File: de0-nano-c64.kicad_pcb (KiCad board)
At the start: 2 copper layers, 79.4 x 75.3 mm, 51 parts, among them J1 GPIO_0, J10 SD_Card, J11 AUDIO, J2 PS2_0, J3 PS2_1, J5 GPIO_1, J6 VGA, J8 JOYSTICK_1, J9 JOYSTICK_2

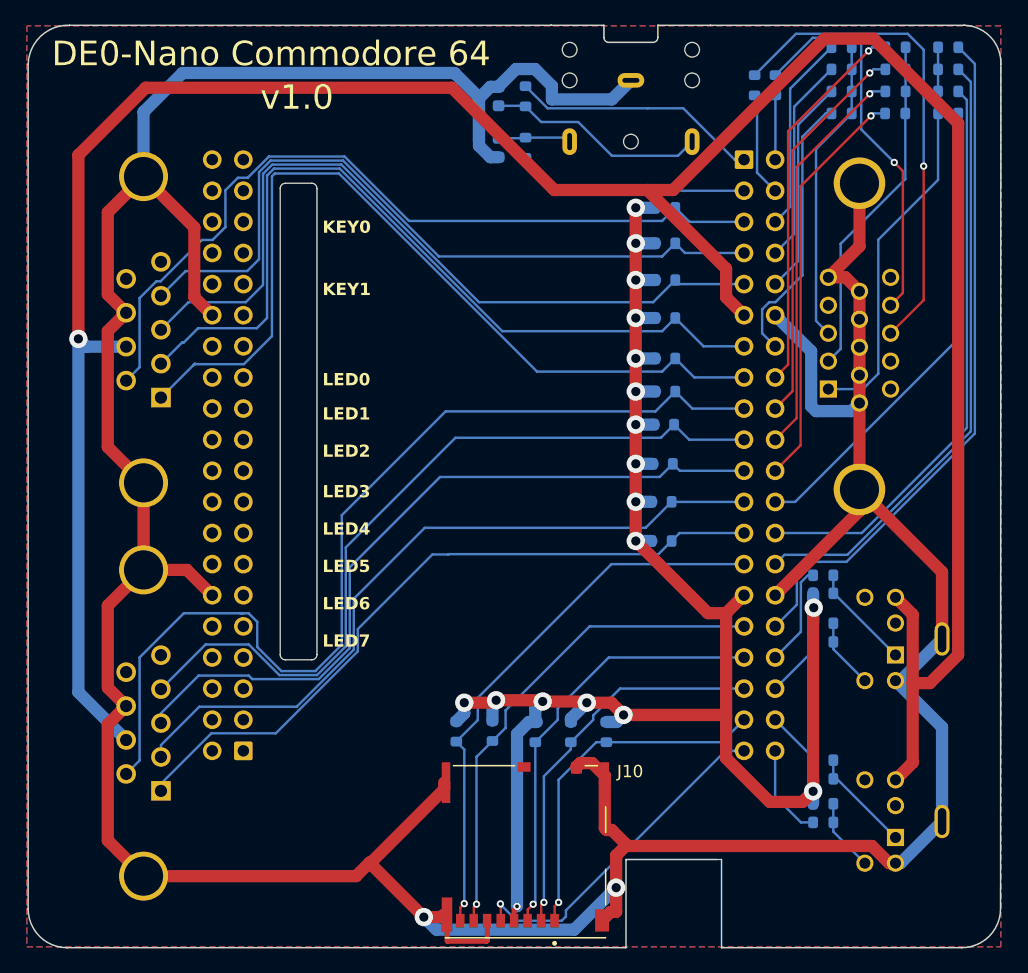
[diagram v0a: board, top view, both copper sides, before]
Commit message: reorder some pins due to input only problem
audio PWM_L/R were assigne to input only pins
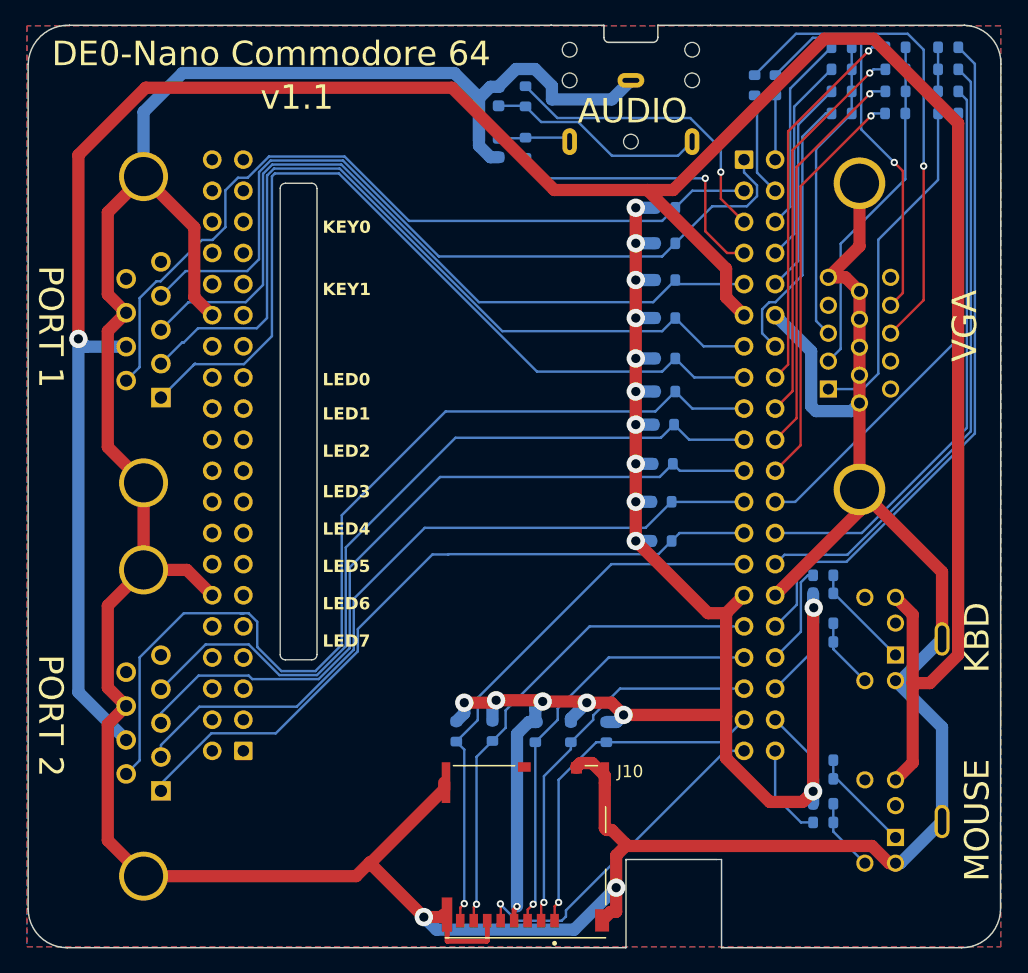
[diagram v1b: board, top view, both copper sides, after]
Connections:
- J5 pad 1: /PWM_L -> /J1_RIGHT
- J5 pad 3: /PWM_R -> /J1_FIRE
- J5 pad 5: /J1_FIRE -> /PWM_L
- J5 pad 7: /J1_RIGHT -> /PWM_R
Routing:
- net /J1_RIGHT: track 60.3 -> 66.1 mm
- net /PWM_R: track 18.9 -> 23.6 mm, vias 0 -> 1
- net /PWM_L: track 20.3 -> 24.8 mm, vias 0 -> 1
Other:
- board text added: "AUDIO"
- board text added: "KBD"
- board text added: "MOUSE"
- board text added: "PORT 1"
- board text added: "PORT 2"
- board text added: "VGA"
- board text added: "v1.1"
- board text removed: "v1.0"
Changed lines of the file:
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@@
       (stroke (width 0.1) (type solid)) (layer "B.Fab"))
     (pad "1" thru_hole roundrect (at 0 0 180) (size 1.524 1.524) (drill 0.9398) (layers "*.Cu" "*.Mask") (roundrect_rratio 0.1)
-      (net 80 "/PWM_L") (pinfunction "Pin_1") (pintype "passive"))
+      (net 67 "/J1_RIGHT") (pinfunction "Pin_1") (pintype "passive"))
     (pad "2" thru_hole circle (at -2.54 0 180) (size 1.524 1.524) (drill 0.9398) (layers "*.Cu" "*.Mask")
       (net 13 "/VS") (pinfunction "Pin_2") (pintype "passive"))
     (pad "3" thru_hole circle (at 0 -2.54 180) (size 1.524 1.524) (drill 0.9398) (layers "*.Cu" "*.Mask")
-      (net 81 "/PWM_R") (pinfunction "Pin_3") (pintype "passive"))
+      (net 68 "/J1_FIRE") (pinfunction "Pin_3") (pintype "passive"))
     (pad "4" thru_hole circle (at -2.54 -2.54 180) (size 1.524 1.524) (drill 0.9398) (layers "*.Cu" "*.Mask")
       (net 12 "/HS") (pinfunction "Pin_4") (pintype "passive"))
     (pad "5" thru_hole circle (at 0 -5.08 180) (size 1.524 1.524) (drill 0.9398) (layers "*.Cu" "*.Mask")
-      (net 68 "/J1_FIRE") (pinfunction "Pin_5") (pintype "passive"))
+      (net 80 "/PWM_L") (pinfunction "Pin_5") (pintype "passive"))
     (pad "6" thru_hole circle (at -2.54 -5.08 180) (size 1.524 1.524) (drill 0.9398) (layers "*.Cu" "*.Mask")
       (net 11 "/B0") (pinfunction "Pin_6") (pintype "passive"))
     (pad "7" thru_hole circle (at 0 -7.62 180) (size 1.524 1.524) (drill 0.9398) (layers "*.Cu" "*.Mask")
-      (net 67 "/J1_RIGHT") (pinfunction "Pin_7") (pintype "passive"))
+      (net 81 "/PWM_R") (pinfunction "Pin_7") (pintype "passive"))
     (pad "8" thru_hole circle (at -2.54 -7.62 180) (size 1.524 1.524) (drill 0.9398) (layers "*.Cu" "*.Mask")
       (net 9 "/B1") (pinfunction "Pin_8") (pintype "passive"))
@@
   (gr_line (start 125.767499 117.240001) (end 125.76802 79.19052)
     (stroke (width 0.05) (type default)) (layer "Edge.Cuts"))
+  (gr_text "PORT 2" (at 105.8545 117.221 270) (layer "F.SilkS")
+    (effects (font (size 2 2) (thickness 0.3)) (justify left bottom))
+  )
   (gr_text "LED6" (at 129.2225 113.665) (layer "F.SilkS")
     (effects (font (size 1 1) (thickness 0.15) bold) (justify left bottom))
   )
+  (gr_text "MOUSE" (at 183.8325 135.763 90) (layer "F.SilkS")
+    (effects (font (size 2 2) (thickness 0.3)) (justify left bottom))
+  )
   (gr_text "LED2" (at 129.2225 101.219) (layer "F.SilkS")
     (effects (font (size 1 1) (thickness 0.15) bold) (justify left bottom))
   )
+  (gr_text "VGA" (at 182.8165 93.345 90) (layer "F.SilkS")
+    (effects (font (size 2 2) (thickness 0.3)) (justify left bottom))
+  )
   (gr_text "LED0" (at 129.2225 95.377) (layer "F.SilkS")
     (effects (font (size 1 1) (thickness 0.15) bold) (justify left bottom))
@@
     (effects (font (size 1 1) (thickness 0.15) bold) (justify left bottom))
   )
+  (gr_text "AUDIO" (at 150.0505 74.041) (layer "F.SilkS")
+    (effects (font (size 2 2) (thickness 0.3)) (justify left bottom))
+  )
   (gr_text "LED3" (at 129.2225 104.521) (layer "F.SilkS")
     (effects (font (size 1 1) (thickness 0.15) bold) (justify left bottom))
@@
     (effects (font (size 1 1) (thickness 0.15) bold) (justify left bottom))
   )
+  (gr_text "PORT 1" (at 105.8545 85.471 270) (layer "F.SilkS")
+    (effects (font (size 2 2) (thickness 0.3)) (justify left bottom))
+  )
   (gr_text "LED5" (at 129.2225 110.617) (layer "F.SilkS")
     (effects (font (size 1 1) (thickness 0.15) bold) (justify left bottom))
   )
-  (gr_text "v1.0" (at 124.1425 71.755) (layer "F.SilkS")
-    (effects (font (size 2 2) (thickness 0.15)) (justify left))
+  (gr_text "v1.1" (at 124.1425 71.755) (layer "F.SilkS")
+    (effects (font (size 2 2) (thickness 0.3)) (justify left))
+  )
+  (gr_text "KBD" (at 183.8325 118.745 90) (layer "F.SilkS")
+    (effects (font (size 2 2) (thickness 0.3)) (justify left bottom))
   )
   (gr_text "DE0-Nano Commodore 64" (at 107.1245 68.199) (layer "F.SilkS")
-    (effects (font (size 2 2) (thickness 0.15)) (justify left))
+    (effects (font (size 2 2) (thickness 0.3)) (justify left))
   )
   (gr_text "USB" (at 131.9925 140.335) (layer "Dwgs.User")
@@
   (segment (start 163.6286 86.995) (end 158.3475 86.995) (width 0.2) (layer "B.Cu") (net 66))
   (segment (start 118.2795 88.473) (end 116.0325 90.72) (width 0.2) (layer "B.Cu") (net 66))
-  (segment (start 158.8075 84.455) (end 158.0175 83.665) (width 0.2) (layer "B.Cu") (net 67))
+  (segment (start 163.6286 76.835) (end 163.6286 77.873105) (width 0.2) (layer "B.Cu") (net 67))
   (segment (start 156.9425 84.74) (end 138.720529 84.74) (width 0.2) (layer "B.Cu") (net 67))
+  (segment (start 164.6906 78.935105) (end 164.6906 79.814895) (width 0.2) (layer "B.Cu") (net 67))
   (segment (start 158.0175 83.665) (end 156.9425 84.74) (width 0.2) (layer "B.Cu") (net 67))
   (segment (start 123.0705 85.933) (end 118.0495 85.933) (width 0.2) (layer "B.Cu") (net 67))
   (segment (start 138.720529 84.74) (end 130.891529 76.911) (width 0.2) (layer "B.Cu") (net 67))
   (segment (start 118.0495 85.933) (end 116.0325 87.95) (width 0.2) (layer "B.Cu") (net 67))
+  (segment (start 161.0375 80.645) (end 158.0175 83.665) (width 0.2) (layer "B.Cu") (net 67))
   (segment (start 124.984052 76.911) (end 124.0385 77.856552) (width 0.2) (layer "B.Cu") (net 67))
-  (segment (start 163.6286 84.455) (end 158.8075 84.455) (width 0.2) (layer "B.Cu") (net 67))
+  (segment (start 164.6906 79.814895) (end 163.860495 80.645) (width 0.2) (layer "B.Cu") (net 67))
+  (segment (start 163.6286 77.873105) (end 164.6906 78.935105) (width 0.2) (layer "B.Cu") (net 67))
   (segment (start 124.0385 84.965) (end 123.0705 85.933) (width 0.2) (layer "B.Cu") (net 67))
+  (segment (start 163.860495 80.645) (end 161.0375 80.645) (width 0.2) (layer "B.Cu") (net 67))
   (segment (start 124.0385 77.856552) (end 124.0385 84.965) (width 0.2) (layer "B.Cu") (net 67))
   (segment (start 130.891529 76.911) (end 124.984052 76.911) (width 0.2) (layer "B.Cu") (net 67))
   (segment (start 120.243895 83.393) (end 119.375135 83.393) (width 0.2) (layer "B.Cu") (net 68))
+  (segment (start 163.6286 79.375) (end 159.4075 79.375) (width 0.2) (layer "B.Cu") (net 68))
   (segment (start 114.2925 88.134365) (end 114.2925 93.775) (width 0.2) (layer "B.Cu") (net 68))
   (segment (start 131.026977 76.584) (end 124.848604 76.584) (width 0.2) (layer "B.Cu") (net 68))
@@
   (segment (start 136.282977 81.84) (end 131.026977 76.584) (width 0.2) (layer "B.Cu") (net 68))
   (segment (start 156.9425 81.84) (end 136.282977 81.84) (width 0.2) (layer "B.Cu") (net 68))
-  (segment (start 163.6286 81.915) (end 159.1675 81.915) (width 0.2) (layer "B.Cu") (net 68))
   (segment (start 123.119604 78.313) (end 122.320105 78.313) (width 0.2) (layer "B.Cu") (net 68))
   (segment (start 122.320105 78.313) (end 121.2925 79.340605) (width 0.2) (layer "B.Cu") (net 68))
+  (segment (start 159.4075 79.375) (end 158.0175 80.765) (width 0.2) (layer "B.Cu") (net 68))
   (segment (start 114.2925 93.775) (end 113.1925 94.875) (width 0.2) (layer "B.Cu") (net 68))
   (segment (start 124.848604 76.584) (end 123.119604 78.313) (width 0.2) (layer "B.Cu") (net 68))
-  (segment (start 159.1675 81.915) (end 158.0175 80.765) (width 0.2) (layer "B.Cu") (net 68))
   (segment (start 121.2925 79.340605) (end 121.2925 82.344395) (width 0.2) (layer "B.Cu") (net 68))
   (segment (start 157.7175 107.965) (end 156.6425 109.04) (width 0.2) (layer "B.Cu") (net 73))
@@
   (segment (start 175.1425 73.065) (end 174.1925 73.065) (width 0.2) (layer "B.Cu") (net 79))
   (segment (start 174.1925 73.065) (end 173.9925 73.265) (width 0.2) (layer "B.Cu") (net 79))
-  (segment (start 155.7735 72.646) (end 158.6735 72.646) (width 0.2) (layer "B.Cu") (net 80))
-  (segment (start 145.7925 70.84) (end 147.5985 72.646) (width 0.2) (layer "B.Cu") (net 80))
-  (segment (start 158.6735 72.646) (end 162.8625 76.835) (width 0.2) (layer "B.Cu") (net 80))
-  (segment (start 147.5985 72.646) (end 155.7735 72.646) (width 0.2) (layer "B.Cu") (net 80))
-  (segment (start 162.8625 76.835) (end 163.6286 76.835) (width 0.2) (layer "B.Cu") (net 80))
-  (segment (start 163.6286 79.375) (end 148.4775 79.375) (width 0.2) (layer "B.Cu") (net 81))
-  (segment (start 148.4775 79.375) (end 145.7925 76.69) (width 0.2) (layer "B.Cu") (net 81))
+  (segment (start 161.7345 80.0209) (end 161.7345 77.851) (width 0.2) (layer "F.Cu") (net 80))
+  (segment (start 163.6286 81.915) (end 161.7345 80.0209) (width 0.2) (layer "F.Cu") (net 80))
+  (via (at 161.7345 77.851) (size 0.6) (drill 0.3) (layers "F.Cu" "B.Cu") (net 80))
+  (segment (start 145.7925 70.84) (end 148.3905 73.438) (width 0.2) (layer "B.Cu") (net 80))
+  (segment (start 161.7345 75.934208) (end 161.7345 77.851) (width 0.2) (layer "B.Cu") (net 80))
+  (segment (start 159.238292 73.438) (end 161.7345 75.934208) (width 0.2) (layer "B.Cu") (net 80))
+  (segment (start 148.3905 73.438) (end 159.238292 73.438) (width 0.2) (layer "B.Cu") (net 80))
+  (segment (start 162.2425 84.455) (end 163.6286 84.455) (width 0.2) (layer "F.Cu") (net 81))
+  (segment (start 160.4645 78.359) (end 160.4645 82.677) (width 0.2) (layer "F.Cu") (net 81))
+  (segment (start 160.4645 82.677) (end 162.2425 84.455) (width 0.2) (layer "F.Cu") (net 81))
+  (via (at 160.4645 78.359) (size 0.6) (drill 0.3) (layers "F.Cu" "B.Cu") (net 81))
+  (segment (start 147.4615 78.359) (end 160.4645 78.359) (width 0.2) (layer "B.Cu") (net 81))
+  (segment (start 145.7925 76.69) (end 147.4615 78.359) (width 0.2) (layer "B.Cu") (net 81))
   (segment (start 141.5725 137.835) (end 141.5725 139.39) (width 0.2) (layer "F.Cu") (net 82))
   (segment (start 141.7925 137.615) (end 141.5725 137.835) (width 0.2) (layer "F.Cu") (net 82))

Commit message: add USB socket for power + add whole cut for dip switches
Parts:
- added J4: USB_A, Connector_USB:USB_A_Molex_67643_Horizontal, B.Cu at (136.0, 78.4)
- moved R22 14.8 mm to (158.6, 79.1), turned to 180 degrees
- moved C1 14.1 mm to (155.6, 79.1), turned to 180 degrees
- moved C2 9.58 mm to (152.6, 79.1), turned to 0 degrees
- moved R23 5.00 mm to (149.6, 79.1), turned to 0 degrees
- moved R29 0.53 mm to (157.2, 81.3)
- moved R28 0.15 mm to (157.2, 83.8)
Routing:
- net /PWM_L: track 24.8 -> 8.00 mm
- net GND: track 335.1 -> 347.8 mm
- net Net-(C1-Pad1): track 18.0 -> 5.76 mm
- net /SD_DAT2: track 29.2 -> 38.4 mm
- net /SD_DAT3: track 32.2 -> 38.5 mm
- net /PWM_R: track 23.6 -> 17.8 mm
- net /SD_CMD: track 35.7 -> 38.6 mm
- net +5V: track 216.7 -> 218.8 mm
- net /SD_CLK: track 28.3 -> 30.4 mm
- net +3V3: track 143.3 -> 145.0 mm
- net /J1_FIRE: track 66.3 -> 66.8 mm
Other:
- outline, holes or cut-outs redrawn
- board text added: "PWR"
